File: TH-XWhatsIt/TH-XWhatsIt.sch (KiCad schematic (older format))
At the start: 36 parts, among them J1 COLUMNS, J12 EXPANSION HEADER, J13 Conn_01x02, J2 ROWS, U1 LM339, U2 MCP4921-EP, U3 74HCT595, U5 74HCT595, U6 LM339, U7 ProMicro, U8 74HCT595

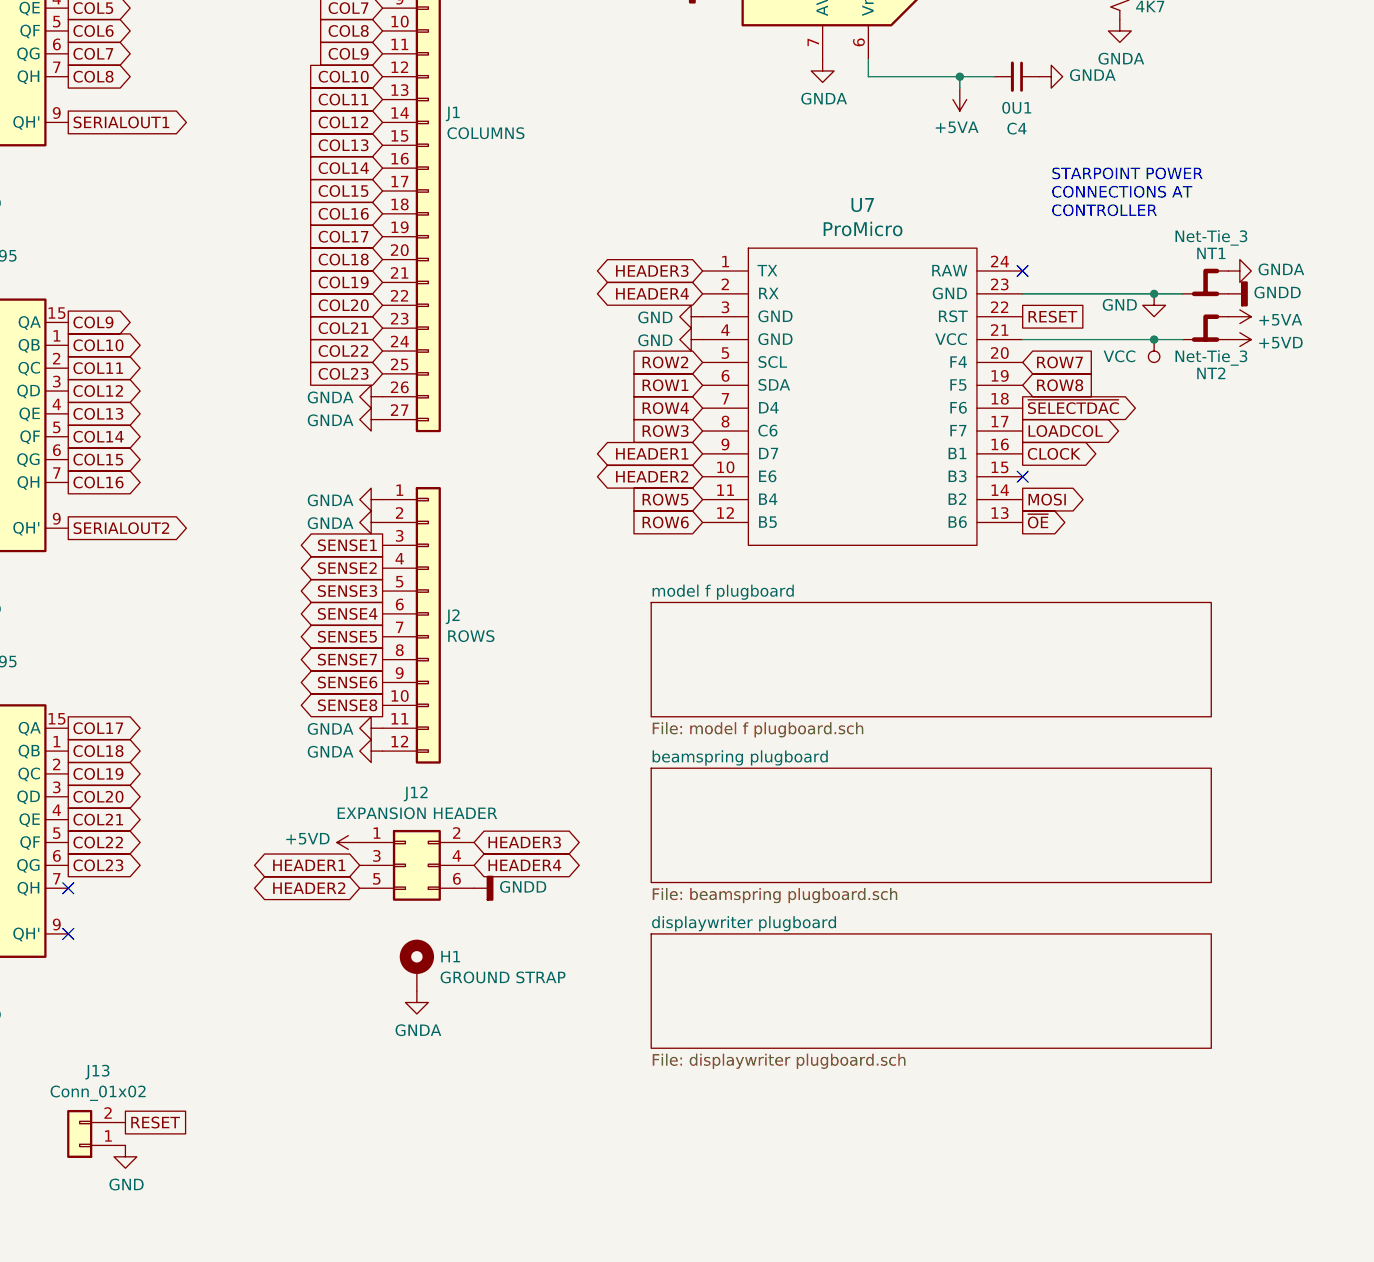
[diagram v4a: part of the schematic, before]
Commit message: Various changes to revision 0.1.1
General:
    Made mounting hole bigger (M3). And moved it a little bit so it doesn't interfere with some components.
    Star ground turned into single ground.
    Ground fills added everywhere.
    Many stitching vias added everywhere.
    Added JLCJLCJLCJLC magic string under pro micro. When ordering from JLCPCB, you can select for Order Number: "Specify Location"
    Bumped version number to 0.1.1
    Added silkscreen to mark rows/columns everywhere.
    Added optional holes for soldering grounding wires everywhere.
Controller:
    Added silkscreen to ease debugging, by marking various important nets.
    Rearranged some traces to maintain better separation between traces, and better ground reference.
Model F plugboard:
    Modified 3.96mm pitch holes, to hole sizes and pad sizes that match original xwhatsit model F controller
    Moved 3.96mm pitch holes closer to the edge, so it doesn't interfere with case in F AT cases.
    Added mounting holes
    Added holes to support 3178 keyboards.
Displaywriter:
    Addes support for more connector types. (The displaywriter daughterboard is now taller)
Beamspring:
    Bugfix to a mistake that only affected people that ran update footprints from library.
Beamship daughterboard:
    Added support for more connectors. Added breakoff-able mounting hole.
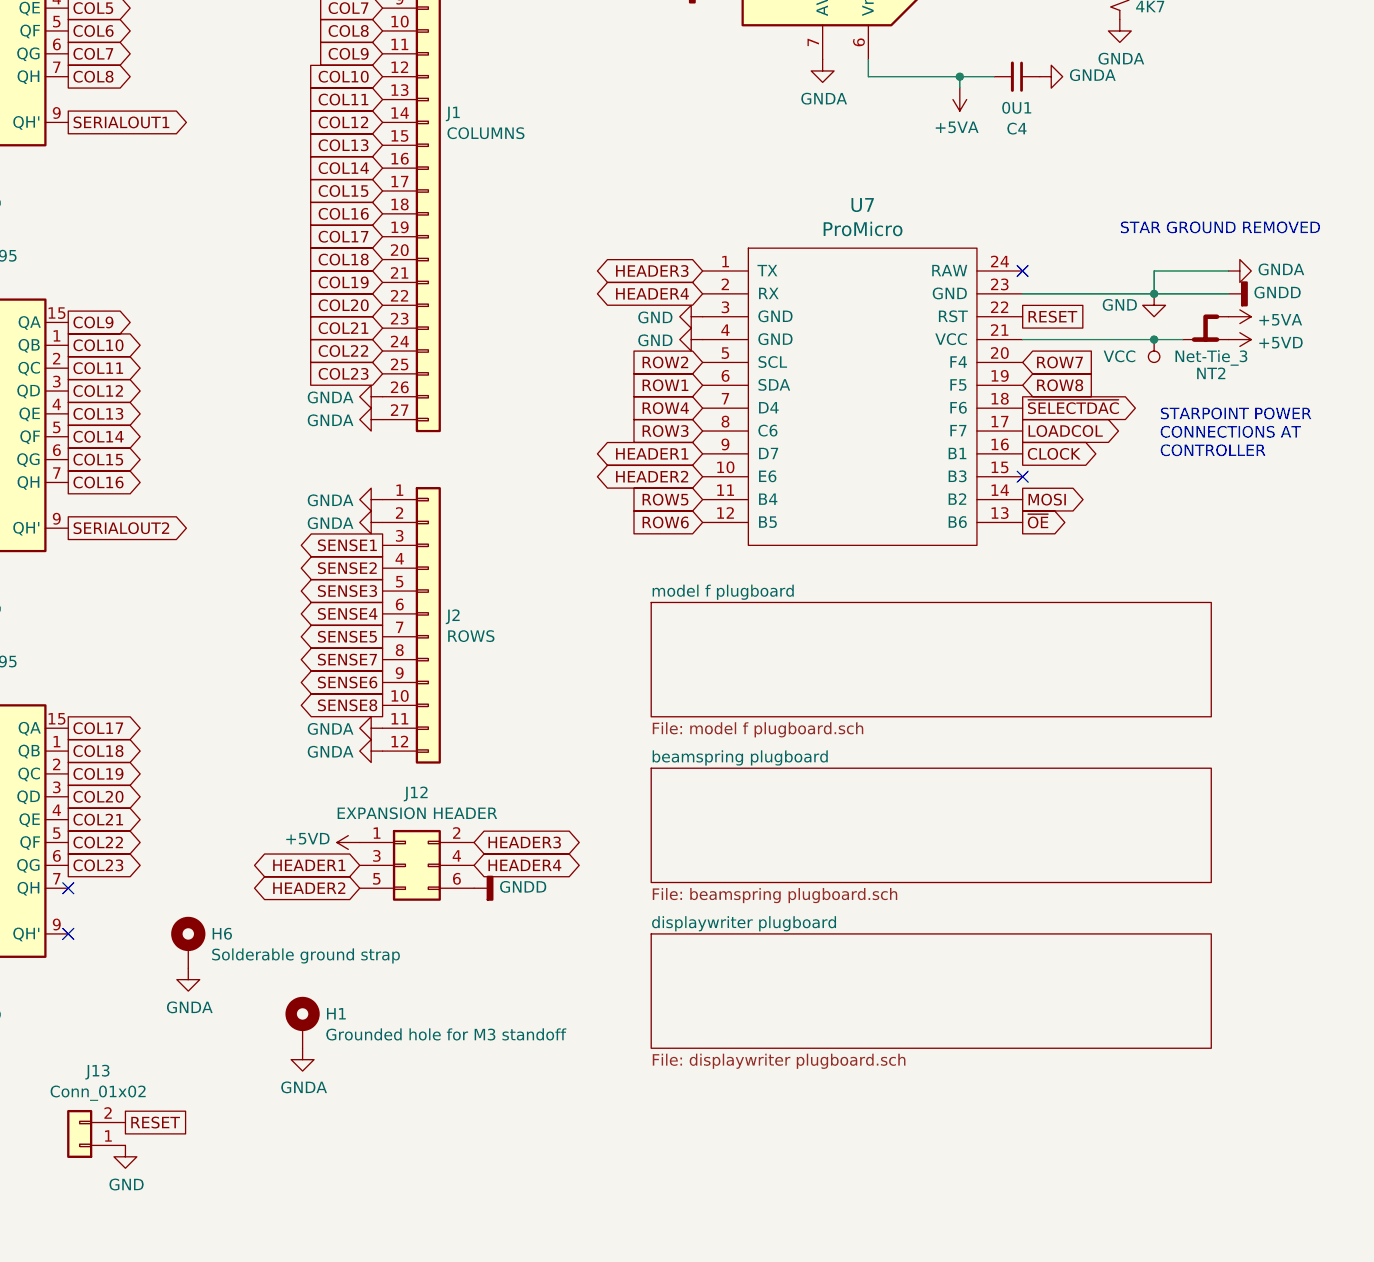
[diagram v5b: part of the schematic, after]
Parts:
- removed NT1: Net-Tie_3, TH-XWhatsIt:NetTie-3_THT_Pad1.0mm_mod_thicker, symbol Device:Net-Tie_3
- added H6: Solderable ground strap, TH-XWhatsIt:ChassisGnd, symbol Mechanical:MountingHole_Pad
- H1: value GROUND STRAP -> Grounded hole for M3 standoff; footprint MountingHole:MountingHole_2.2mm_M2_Pad_Via -> MountingHole:MountingHole_3.2mm_M3_Pad_Via
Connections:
- net GNDA is gone; now on net GND: C10.1, C4.1, C9.1, H1.1, J1.1 (Pin_1), J1.2 (Pin_2), J1.26 (Pin_26), J1.27 (Pin_27), J2.1 (Pin_1), J2.11 (Pin_11), J2.12 (Pin_12), J2.2 (Pin_2), R2.2, R5.1, U1.12 (V-), U2.7 (AVSS), U6.12 (V-)
- net GNDD is gone; now on net GND: C3.1, C5.1, C7.1, C8.1, J12.6 (Pin_6), U2.5 (~LDAC~), U3.8 (GND), U5.8 (GND), U8.8 (GND)
- net GND: now also H6.1
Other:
- note added: "STAR GROUND REMOVED"
- moved on the sheet: H1
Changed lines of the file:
@@
 Title "TH-XWhatsIt combined beamspring and model f controller"
 Date "2020-01-31"
-Rev "0.0.3"
+Rev "0.1.1"
 Comp "Rainy Day Plans"
 Comment1 ""
@@
 	0    1    1    0
 $EndComp
-Wire Wire Line
-	10550 2825 10425 2825
-Text Notes 9975 2500 0    50   ~ 0
+Text Notes 10450 3550 0    50   ~ 0
 STARPOINT POWER\nCONNECTIONS AT\nCONTROLLER
 $Comp
 L Mechanical:MountingHole_Pad H1
 U 1 1 5E90A976
-P 7200 5775
-F 0 "H1" H 7300 5824 50  0000 L CNN
-F 1 "GROUND STRAP" H 7300 5733 50  0000 L CNN
-F 2 "MountingHole:MountingHole_2.2mm_M2_Pad_Via" H 7200 5775 50  0001 C CNN
-F 3 "~" H 7200 5775 50  0001 C CNN
-	1    7200 5775
+P 6700 6025
+F 0 "H1" H 6800 6074 50  0000 L CNN
+F 1 "Grounded hole for M3 standoff" H 6800 5983 50  0000 L CNN
+F 2 "MountingHole:MountingHole_3.2mm_M3_Pad_Via" H 6700 6025 50  0001 C CNN
+F 3 "~" H 6700 6025 50  0001 C CNN
+	1    6700 6025
 	1    0    0    -1
 $EndComp
@@
 L power:GNDA #PWR0148
 U 1 1 5E90B41B
-P 7200 5875
-F 0 "#PWR0148" H 7200 5625 50  0001 C CNN
-F 1 "GNDA" H 7205 5702 50  0000 C CNN
-F 2 "" H 7200 5875 50  0001 C CNN
-F 3 "" H 7200 5875 50  0001 C CNN
-	1    7200 5875
+P 6700 6125
+F 0 "#PWR0148" H 6700 5875 50  0001 C CNN
+F 1 "GNDA" H 6705 5952 50  0000 C CNN
+F 2 "" H 6700 6125 50  0001 C CNN
+F 3 "" H 6700 6125 50  0001 C CNN
+	1    6700 6125
 	1    0    0    -1
 $EndComp
@@
 $EndComp
 $Comp
-L Device:Net-Tie_3 NT1
-U 1 1 5F549EF2
-P 10650 2825
-F 0 "NT1" H 10625 2650 50  0000 C CNN
-F 1 "Net-Tie_3" H 10625 2575 50  0000 C CNN
-F 2 "TH-XWhatsIt:NetTie-3_THT_Pad1.0mm_mod_thicker" H 10650 2825 50  0001 C CNN
-F 3 "~" H 10650 2825 50  0001 C CNN
-	1    10650 2825
-	-1   0    0    1
-$EndComp
-$Comp
 L power:+5VD #PWR0110
 U 1 1 5E81915B
@@
 Wire Wire Line
 	1425 3275 1775 3275
+Wire Wire Line
+	10425 2825 10750 2825
+Wire Wire Line
+	10750 2725 10425 2725
+Wire Wire Line
+	10425 2725 10425 2825
+Text Notes 10275 2575 0    50   ~ 0
+STAR GROUND REMOVED
+$Comp
+L Mechanical:MountingHole_Pad H6
+U 1 1 5FBAD0AC
+P 6200 5675
+F 0 "H6" H 6300 5724 50  0000 L CNN
+F 1 "Solderable ground strap" H 6300 5633 50  0000 L CNN
+F 2 "TH-XWhatsIt:ChassisGnd" H 6200 5675 50  0001 C CNN
+F 3 "~" H 6200 5675 50  0001 C CNN
+	1    6200 5675
+	1    0    0    -1
+$EndComp
+$Comp
+L power:GNDA #PWR0127
+U 1 1 5FBAD3F8
+P 6200 5775
+F 0 "#PWR0127" H 6200 5525 50  0001 C CNN
+F 1 "GNDA" H 6205 5602 50  0000 C CNN
+F 2 "" H 6200 5775 50  0001 C CNN
+F 3 "" H 6200 5775 50  0001 C CNN
+	1    6200 5775
+	1    0    0    -1
+$EndComp
 $EndSCHEMATC
